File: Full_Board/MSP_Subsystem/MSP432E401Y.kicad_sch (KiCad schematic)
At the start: 4 parts, among them J1-J3 Conn_01x10, J4-J2 Conn_01x10, J5-J7 Conn_01x10, J8-J6 Conn_01x10

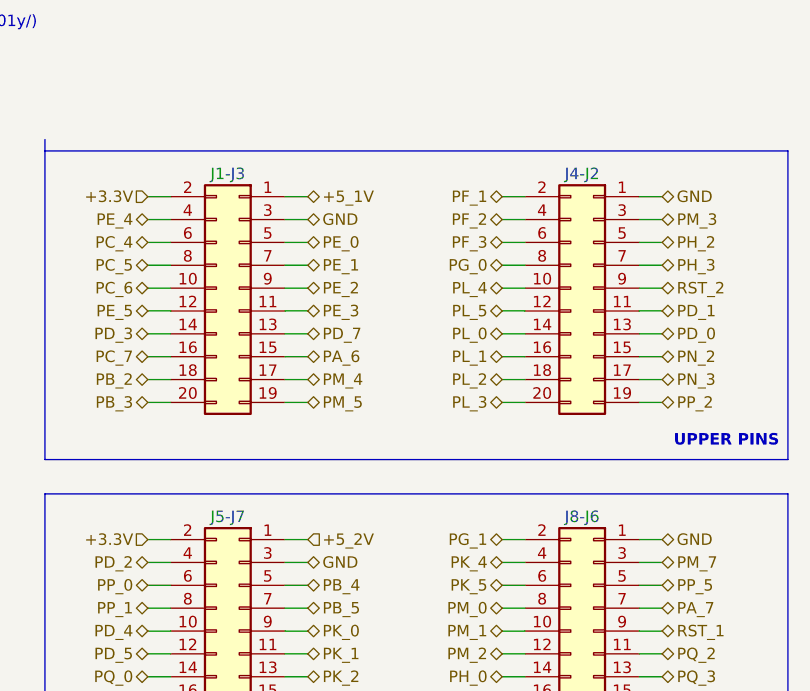
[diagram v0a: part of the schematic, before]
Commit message: Replace small resistors/capacitors with through-hole; fix DRC aside from electromagnet and MUXes
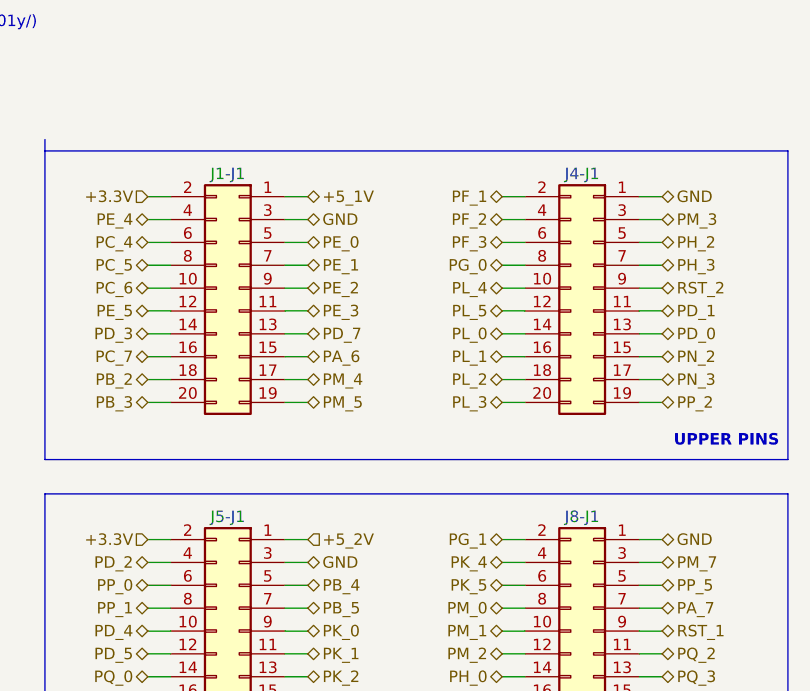
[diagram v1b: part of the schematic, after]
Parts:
- renumbered J1-J3 to J1-J1, J4-J2 to J4-J1, J5-J7 to J5-J1, J8-J6 to J8-J1
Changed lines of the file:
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@@
   (symbol (lib_id "Connector_Generic:Conn_02x10_Odd_Even") (at 170.18 71.12 0) (mirror y) (unit 1)
     (in_bom yes) (on_board yes)
-    (property "Reference" "J4-J2" (id 0) (at 168.91 58.42 0))
+    (property "Reference" "J4-J1" (id 0) (at 168.91 58.42 0))
     (property "Value" "Conn_01x10" (id 1) (at 172.72 87.63 0)
       (effects (font (size 1.27 1.27)) hide)
@@
   (symbol (lib_id "Connector_Generic:Conn_02x10_Odd_Even") (at 130.81 109.22 0) (mirror y) (unit 1)
     (in_bom yes) (on_board yes)
-    (property "Reference" "J5-J7" (id 0) (at 129.54 96.52 0))
+    (property "Reference" "J5-J1" (id 0) (at 129.54 96.52 0))
     (property "Value" "Conn_01x10" (id 1) (at 128.27 113.03 0)
       (effects (font (size 1.27 1.27)) (justify left) hide)
@@
   (symbol (lib_id "Connector_Generic:Conn_02x10_Odd_Even") (at 170.18 109.22 0) (mirror y) (unit 1)
     (in_bom yes) (on_board yes)
-    (property "Reference" "J8-J6" (id 0) (at 168.91 96.52 0))
+    (property "Reference" "J8-J1" (id 0) (at 168.91 96.52 0))
     (property "Value" "Conn_01x10" (id 1) (at 172.72 125.73 0)
       (effects (font (size 1.27 1.27)) hide)
@@
   (symbol (lib_id "Connector_Generic:Conn_02x10_Odd_Even") (at 130.81 71.12 0) (mirror y) (unit 1)
     (in_bom yes) (on_board yes)
-    (property "Reference" "J1-J3" (id 0) (at 129.54 58.42 0))
+    (property "Reference" "J1-J1" (id 0) (at 129.54 58.42 0))
     (property "Value" "Conn_01x10" (id 1) (at 128.27 74.93 0)
       (effects (font (size 1.27 1.27)) (justify left) hide)

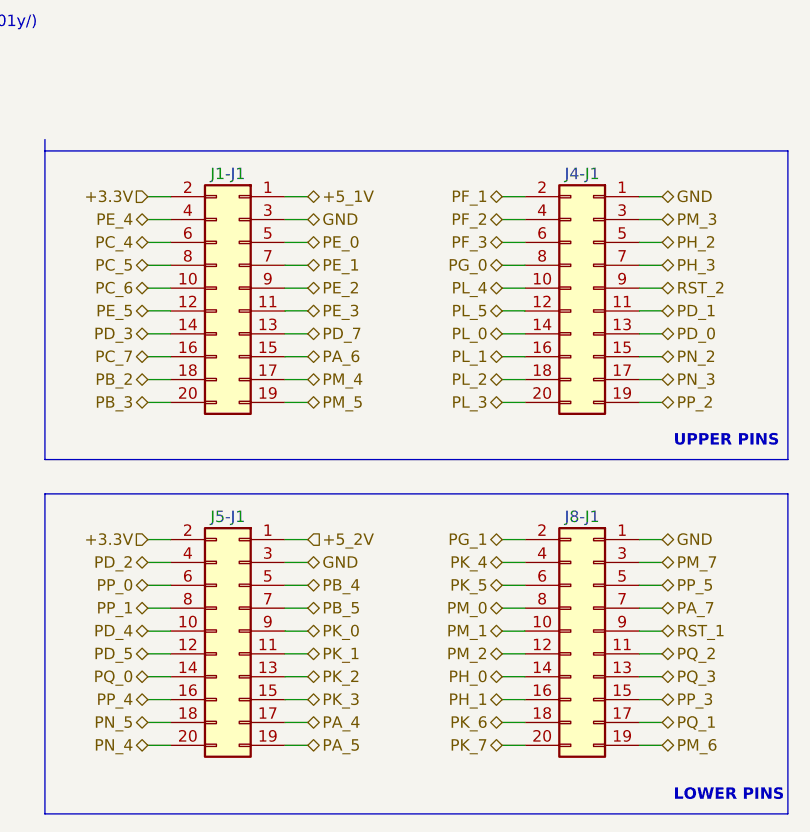
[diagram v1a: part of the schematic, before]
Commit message: Cleanup all schematics and project libs
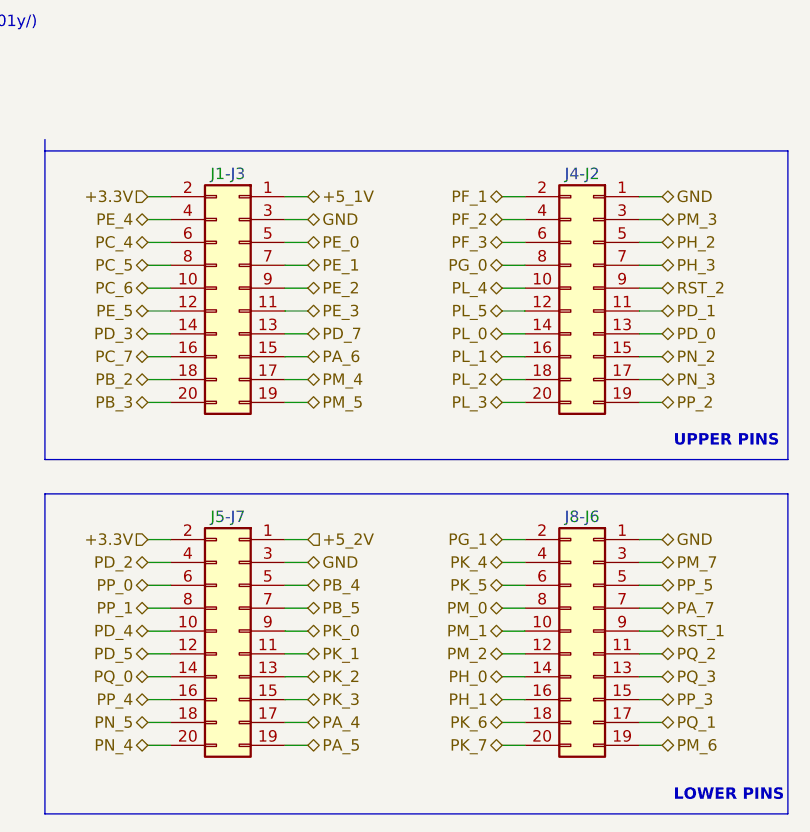
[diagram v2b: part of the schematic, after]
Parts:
- J1-J3: renamed from J1-J1; symbol Connector_Generic:Conn_02x10_Odd_Even -> PPTC102LFBN-RC:PPTC102LFBN-RC; Digikey Link (none) -> https://media.digikey.com/pdf/Data%20Sheets/Sullins%20PDFs/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; Digikey link https://www.digikey.com/en/products/detail/sullins-connecto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 -> (none); Mouser Link (none) -> https://www.mouser.com/ProductDetail/Harwin/M50-3001045?qs=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; Mouser link https://www.mouser.com/ProductDetail/Harwin/M50-3001045?qs=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 -> (none)
- J4-J2: renamed from J4-J1; symbol Connector_Generic:Conn_02x10_Odd_Even -> PPTC102LFBN-RC:PPTC102LFBN-RC; Digikey Link (none) -> https://media.digikey.com/pdf/Data%20Sheets/Sullins%20PDFs/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; Digikey link https://www.digikey.com/en/products/detail/sullins-connecto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 -> (none); Mouser Link (none) -> https://www.mouser.com/ProductDetail/Harwin/M50-3001045?qs=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; Mouser link https://www.mouser.com/ProductDetail/Harwin/M50-3001045?qs=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 -> (none)
- J5-J7: renamed from J5-J1; symbol Connector_Generic:Conn_02x10_Odd_Even -> PPTC102LFBN-RC:PPTC102LFBN-RC; Digikey Link (none) -> https://media.digikey.com/pdf/Data%20Sheets/Sullins%20PDFs/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; Digikey link https://www.digikey.com/en/products/detail/sullins-connecto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 -> (none); Mouser Link (none) -> https://www.mouser.com/ProductDetail/Harwin/M50-3001045?qs=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; Mouser link https://www.mouser.com/ProductDetail/Harwin/M50-3001045?qs=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 -> (none)
- J8-J6: renamed from J8-J1; symbol Connector_Generic:Conn_02x10_Odd_Even -> PPTC102LFBN-RC:PPTC102LFBN-RC; Digikey Link (none) -> https://media.digikey.com/pdf/Data%20Sheets/Sullins%20PDFs/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; Digikey link https://www.digikey.com/en/products/detail/sullins-connecto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 -> (none); Mouser Link (none) -> https://www.mouser.com/ProductDetail/Harwin/M50-3001045?qs=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; Mouser link https://www.mouser.com/ProductDetail/Harwin/M50-3001045?qs=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 -> (none)
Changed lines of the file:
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@@
     (effects (font (size 1.27 1.27)) (justify right))
   )
-  (symbol (lib_id "Connector_Generic:Conn_02x10_Odd_Even") (at 170.18 71.12 0) (mirror y) (unit 1)
+  (symbol (lib_id "PPTC102LFBN-RC:PPTC102LFBN-RC") (at 168.91 86.36 0) (mirror y) (unit 1)
     (in_bom yes) (on_board yes)
-    (property "Reference" "J4-J1" (id 0) (at 168.91 58.42 0))
-    (property "Value" "Conn_01x10" (id 1) (at 172.72 87.63 0)
+    (property "Reference" "J4-J2" (id 0) (at 168.91 58.42 0))
+    (property "Value" "Conn_01x10" (id 1) (at 171.45 102.87 0)
       (effects (font (size 1.27 1.27)) hide)
     )
-    (property "Footprint" "Connector_PinSocket_2.54mm:PinSocket_2x10_P2.54mm_Vertical" (id 2) (at 170.18 71.12 0)
+    (property "Footprint" "Connector_PinSocket_2.54mm:PinSocket_2x10_P2.54mm_Vertical" (id 2) (at 168.91 86.36 0)
       (effects (font (size 1.27 1.27)) hide)
     )
-    (property "Datasheet" "~" (id 3) (at 170.18 71.12 0)
+    (property "Datasheet" "https://media.digikey.com/pdf/Data%20Sheets/Sullins%20PDFs/Female_Headers.100_DS.pdf" (id 3) (at 168.91 86.36 0)
       (effects (font (size 1.27 1.27)) hide)
     )
-    (property "Digikey Part Number" "S7078-ND" (id 4) (at 170.18 71.12 0)
+    (property "Digikey Part Number" "S7078-ND" (id 4) (at 168.91 86.36 0)
       (effects (font (size 1.27 1.27)) hide)
     )
-    (property "Digikey link" "https://www.digikey.com/en/products/detail/sullins-connector-solutions/PPTC102LFBN-RC/810216" (id 5) (at 170.18 71.12 0)
+    (property "Manufacturer's Part Number" "PPTC102LFBN-RC" (id 6) (at 168.91 86.36 0)
       (effects (font (size 1.27 1.27)) hide)
     )
-    (property "Manufacturer's Part Number" "PPTC102LFBN-RC" (id 6) (at 170.18 71.12 0)
+    (property "Mouser Part Number" "855-M50-3001045" (id 7) (at 168.91 86.36 0)
       (effects (font (size 1.27 1.27)) hide)
     )
-    (property "Mouser Part Number" "855-M50-3001045" (id 7) (at 170.18 71.12 0)
+    (property "Digikey Link" "https://media.digikey.com/pdf/Data%20Sheets/Sullins%20PDFs/Female_Headers.100_DS.pdf" (id 9) (at 168.91 86.36 0)
       (effects (font (size 1.27 1.27)) hide)
     )
-    (property "Mouser link" "https://www.mouser.com/ProductDetail/Harwin/M50-3001045?qs=sGAEpiMZZMvlX3nhDDO4ACiIlPQK9Fd3x0shJJA6fS8%3D" (id 8) (at 170.18 71.12 0)
+    (property "Mouser Link" "https://www.mouser.com/ProductDetail/Harwin/M50-3001045?qs=9fQaSFfsqsy4fizyLh4kvw%3D%3D" (id 10) (at 168.91 86.36 0)
       (effects (font (size 1.27 1.27)) hide)
     )
@@
     (pin "9")
   )
-  (symbol (lib_id "Connector_Generic:Conn_02x10_Odd_Even") (at 130.81 109.22 0) (mirror y) (unit 1)
+  (symbol (lib_id "PPTC102LFBN-RC:PPTC102LFBN-RC") (at 129.54 124.46 0) (mirror y) (unit 1)
     (in_bom yes) (on_board yes)
-    (property "Reference" "J5-J1" (id 0) (at 129.54 96.52 0))
-    (property "Value" "Conn_01x10" (id 1) (at 128.27 113.03 0)
+    (property "Reference" "J5-J7" (id 0) (at 129.54 96.52 0))
+    (property "Value" "Conn_01x10" (id 1) (at 127 128.27 0)
       (effects (font (size 1.27 1.27)) (justify left) hide)
     )
-    (property "Footprint" "Connector_PinSocket_2.54mm:PinSocket_2x10_P2.54mm_Vertical" (id 2) (at 130.81 110.49 0)
+    (property "Footprint" "Connector_PinSocket_2.54mm:PinSocket_2x10_P2.54mm_Vertical" (id 2) (at 129.54 124.46 0)
       (effects (font (size 1.27 1.27)) hide)
     )
-    (property "Datasheet" "~" (id 3) (at 130.81 109.22 0)
+    (property "Datasheet" "https://media.digikey.com/pdf/Data%20Sheets/Sullins%20PDFs/Female_Headers.100_DS.pdf" (id 3) (at 129.54 124.46 0)
       (effects (font (size 1.27 1.27)) hide)
     )
-    (property "Digikey Part Number" "S7078-ND" (id 4) (at 130.81 109.22 0)
+    (property "Digikey Part Number" "S7078-ND" (id 4) (at 129.54 124.46 0)
       (effects (font (size 1.27 1.27)) hide)
     )
-    (property "Digikey link" "https://www.digikey.com/en/products/detail/sullins-connector-solutions/PPTC102LFBN-RC/810216" (id 5) (at 130.81 109.22 0)
+    (property "Manufacturer's Part Number" "PPTC102LFBN-RC" (id 6) (at 129.54 124.46 0)
       (effects (font (size 1.27 1.27)) hide)
     )
-    (property "Manufacturer's Part Number" "PPTC102LFBN-RC" (id 6) (at 130.81 109.22 0)
+    (property "Mouser Part Number" "855-M50-3001045" (id 7) (at 129.54 124.46 0)
       (effects (font (size 1.27 1.27)) hide)
     )
-    (property "Mouser Part Number" "855-M50-3001045" (id 7) (at 130.81 109.22 0)
+    (property "Digikey Link" "https://media.digikey.com/pdf/Data%20Sheets/Sullins%20PDFs/Female_Headers.100_DS.pdf" (id 9) (at 129.54 124.46 0)
       (effects (font (size 1.27 1.27)) hide)
     )
-    (property "Mouser link" "https://www.mouser.com/ProductDetail/Harwin/M50-3001045?qs=sGAEpiMZZMvlX3nhDDO4ACiIlPQK9Fd3x0shJJA6fS8%3D" (id 8) (at 130.81 109.22 0)
+    (property "Mouser Link" "https://www.mouser.com/ProductDetail/Harwin/M50-3001045?qs=9fQaSFfsqsy4fizyLh4kvw%3D%3D" (id 10) (at 129.54 124.46 0)
       (effects (font (size 1.27 1.27)) hide)
     )
@@
     (pin "9")
   )
-  (symbol (lib_id "Connector_Generic:Conn_02x10_Odd_Even") (at 170.18 109.22 0) (mirror y) (unit 1)
+  (symbol (lib_id "PPTC102LFBN-RC:PPTC102LFBN-RC") (at 168.91 124.46 0) (mirror y) (unit 1)
     (in_bom yes) (on_board yes)
-    (property "Reference" "J8-J1" (id 0) (at 168.91 96.52 0))
-    (property "Value" "Conn_01x10" (id 1) (at 172.72 125.73 0)
+    (property "Reference" "J8-J6" (id 0) (at 168.91 96.52 0))
+    (property "Value" "Conn_01x10" (id 1) (at 171.45 140.97 0)
       (effects (font (size 1.27 1.27)) hide)
     )
-    (property "Footprint" "Connector_PinSocket_2.54mm:PinSocket_2x10_P2.54mm_Vertical" (id 2) (at 170.18 110.49 0)
+    (property "Footprint" "Connector_PinSocket_2.54mm:PinSocket_2x10_P2.54mm_Vertical" (id 2) (at 168.91 124.46 0)
       (effects (font (size 1.27 1.27)) hide)
     )
-    (property "Datasheet" "~" (id 3) (at 170.18 109.22 0)
+    (property "Datasheet" "https://media.digikey.com/pdf/Data%20Sheets/Sullins%20PDFs/Female_Headers.100_DS.pdf" (id 3) (at 168.91 124.46 0)
       (effects (font (size 1.27 1.27)) hide)
     )
-    (property "Digikey Part Number" "S7078-ND" (id 4) (at 170.18 109.22 0)
+    (property "Digikey Part Number" "S7078-ND" (id 4) (at 168.91 124.46 0)
       (effects (font (size 1.27 1.27)) hide)
     )
-    (property "Digikey link" "https://www.digikey.com/en/products/detail/sullins-connector-solutions/PPTC102LFBN-RC/810216" (id 5) (at 170.18 109.22 0)
+    (property "Manufacturer's Part Number" "PPTC102LFBN-RC" (id 6) (at 168.91 124.46 0)
       (effects (font (size 1.27 1.27)) hide)
     )
-    (property "Manufacturer's Part Number" "PPTC102LFBN-RC" (id 6) (at 170.18 109.22 0)
+    (property "Mouser Part Number" "855-M50-3001045" (id 7) (at 168.91 124.46 0)
       (effects (font (size 1.27 1.27)) hide)
     )
-    (property "Mouser Part Number" "855-M50-3001045" (id 7) (at 170.18 109.22 0)
+    (property "Digikey Link" "https://media.digikey.com/pdf/Data%20Sheets/Sullins%20PDFs/Female_Headers.100_DS.pdf" (id 9) (at 168.91 124.46 0)
       (effects (font (size 1.27 1.27)) hide)
     )
-    (property "Mouser link" "https://www.mouser.com/ProductDetail/Harwin/M50-3001045?qs=sGAEpiMZZMvlX3nhDDO4ACiIlPQK9Fd3x0shJJA6fS8%3D" (id 8) (at 170.18 109.22 0)
+    (property "Mouser Link" "https://www.mouser.com/ProductDetail/Harwin/M50-3001045?qs=9fQaSFfsqsy4fizyLh4kvw%3D%3D" (id 10) (at 168.91 124.46 0)
       (effects (font (size 1.27 1.27)) hide)
     )
@@
     (pin "9")
   )
-  (symbol (lib_id "Connector_Generic:Conn_02x10_Odd_Even") (at 130.81 71.12 0) (mirror y) (unit 1)
+  (symbol (lib_id "PPTC102LFBN-RC:PPTC102LFBN-RC") (at 129.54 86.36 0) (mirror y) (unit 1)
     (in_bom yes) (on_board yes)
-    (property "Reference" "J1-J1" (id 0) (at 129.54 58.42 0))
-    (property "Value" "Conn_01x10" (id 1) (at 128.27 74.93 0)
+    (property "Reference" "J1-J3" (id 0) (at 129.54 58.42 0))
+    (property "Value" "Conn_01x10" (id 1) (at 127 90.17 0)
       (effects (font (size 1.27 1.27)) (justify left) hide)
     )
-    (property "Footprint" "Connector_PinSocket_2.54mm:PinSocket_2x10_P2.54mm_Vertical" (id 2) (at 130.81 71.12 0)
+    (property "Footprint" "Connector_PinSocket_2.54mm:PinSocket_2x10_P2.54mm_Vertical" (id 2) (at 129.54 86.36 0)
       (effects (font (size 1.27 1.27)) hide)
     )
-    (property "Datasheet" "~" (id 3) (at 130.81 71.12 0)
+    (property "Datasheet" "https://media.digikey.com/pdf/Data%20Sheets/Sullins%20PDFs/Female_Headers.100_DS.pdf" (id 3) (at 129.54 86.36 0)
       (effects (font (size 1.27 1.27)) hide)
     )
-    (property "Digikey Part Number" "S7078-ND" (id 4) (at 130.81 71.12 0)
+    (property "Digikey Part Number" "S7078-ND" (id 4) (at 129.54 86.36 0)
       (effects (font (size 1.27 1.27)) hide)
     )
-    (property "Digikey link" "https://www.digikey.com/en/products/detail/sullins-connector-solutions/PPTC102LFBN-RC/810216" (id 5) (at 130.81 71.12 0)
+    (property "Manufacturer's Part Number" "PPTC102LFBN-RC" (id 6) (at 129.54 86.36 0)
       (effects (font (size 1.27 1.27)) hide)
     )
-    (property "Manufacturer's Part Number" "PPTC102LFBN-RC" (id 6) (at 130.81 71.12 0)
+    (property "Mouser Part Number" "855-M50-3001045" (id 7) (at 129.54 86.36 0)
       (effects (font (size 1.27 1.27)) hide)
     )
-    (property "Mouser Part Number" "855-M50-3001045" (id 7) (at 130.81 71.12 0)
+    (property "Digikey Link" "https://media.digikey.com/pdf/Data%20Sheets/Sullins%20PDFs/Female_Headers.100_DS.pdf" (id 9) (at 129.54 86.36 0)
       (effects (font (size 1.27 1.27)) hide)
     )
-    (property "Mouser link" "https://www.mouser.com/ProductDetail/Harwin/M50-3001045?qs=sGAEpiMZZMvlX3nhDDO4ACiIlPQK9Fd3x0shJJA6fS8%3D" (id 8) (at 130.81 71.12 0)
+    (property "Mouser Link" "https://www.mouser.com/ProductDetail/Harwin/M50-3001045?qs=9fQaSFfsqsy4fizyLh4kvw%3D%3D" (id 10) (at 129.54 86.36 0)
       (effects (font (size 1.27 1.27)) hide)
     )
